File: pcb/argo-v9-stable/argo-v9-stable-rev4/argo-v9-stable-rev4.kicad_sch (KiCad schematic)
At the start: 131 parts, among them IC2 MP2672GD-0000, J1 Sparkfun_NEO-N9M-SMA, J2 USB4125-GF-A, J3 LED_power_button_RGB_LED, J4 Conn_I2C_Molex_705450003, J5 Conn_I2C_Molex_705450003, K1 PRL3-5V-DC-1A, Q1 BSD840N, Q2 BSD840N, SW1 ON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

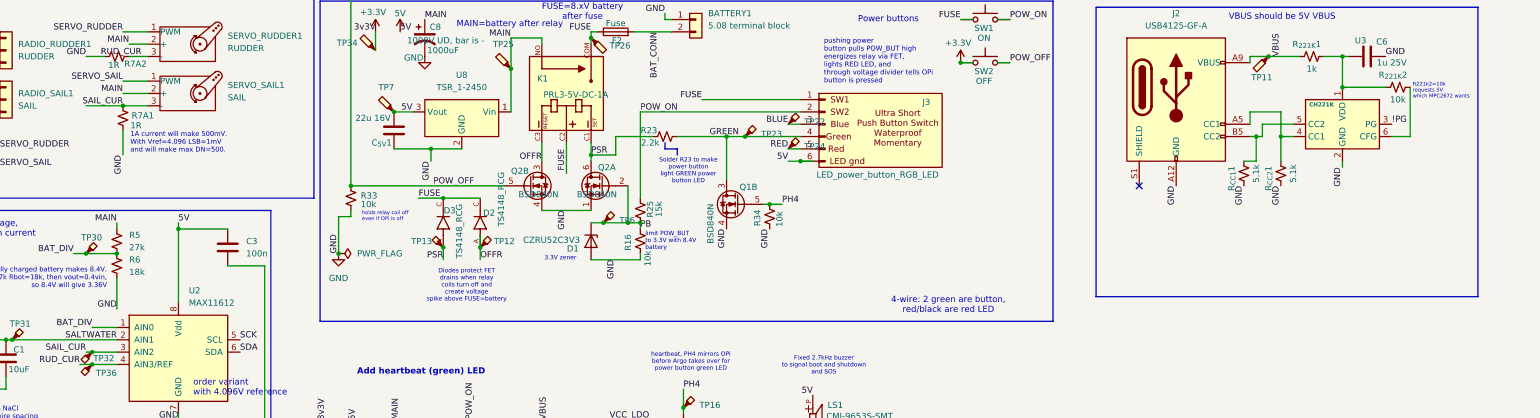
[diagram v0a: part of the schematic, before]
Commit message: add testpoints for CHG, CC1/2
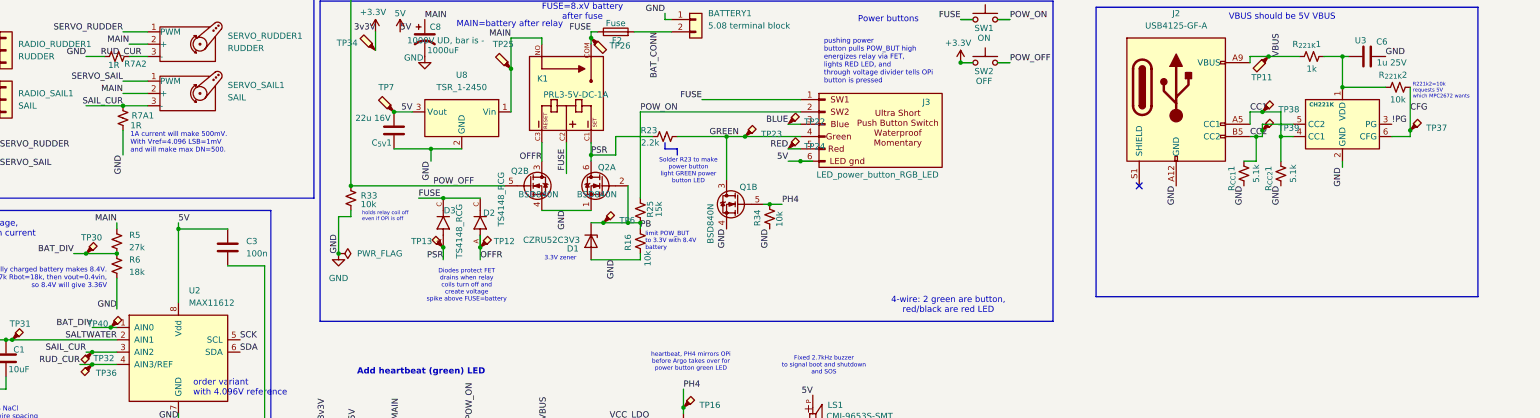
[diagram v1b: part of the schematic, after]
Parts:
- added TP37, TP38, TP39, TP40: TestPoint_Probe_autonamed, Argo footprint Library:TestPoint_scope_small_autonamed, symbol argo-v9:TestPoint_Probe_small_autonamed
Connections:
- net BAT_DIV: now also TP40.1
- net CC2: now reaches J2.B5 (CC2), R_{CC1}1.2, U3.5 (CC2)
- net CC2: now also TP39.1
- net CC1: now reaches J2.A5 (CC1), R_{CC2}1.2, U3.4 (CC1)
- net CC1: now also TP38.1
- net CFG: now reaches R_{221K}2.2, U3.6 (CFG)
- net CFG: now also TP37.1

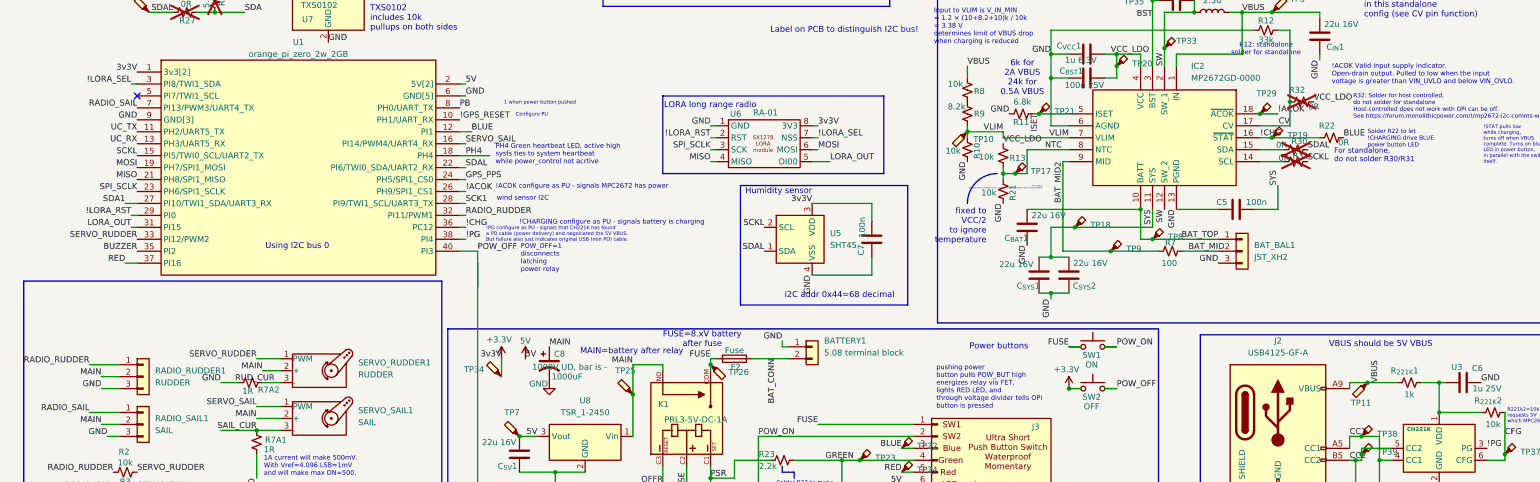
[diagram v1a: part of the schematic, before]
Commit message: more testpoints and cleanup text. Add libs
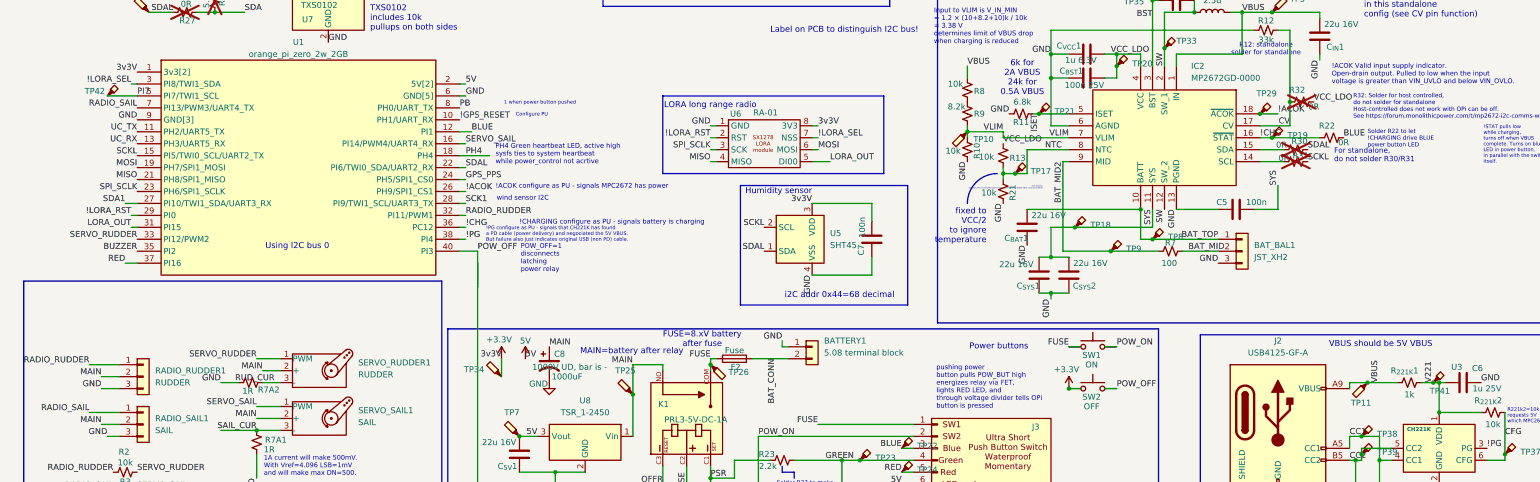
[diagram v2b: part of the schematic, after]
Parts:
- added TP41, TP42: TestPoint_Probe_autonamed, Argo footprint Library:TestPoint_scope_small_autonamed, symbol argo-v9:TestPoint_Probe_small_autonamed
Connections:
- net V221: now reaches C6.1, R_{221K}1.2, R_{221K}2.1, U3.1 (VDD)
- net V221: now also TP41.1
- net PI7: now reaches U1.5 (PI7/TWI1_SCL)
- net PI7: now also TP42.1
- no-connect marks 2 -> 1
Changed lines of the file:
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@@
 	)
 	(junction
+		(at 370.84 167.64)
+		(diameter 0)
+		(color 0 0 0 0)
+	)
+	(junction
 		(at 313.69 96.52)
 		(diameter 0)
@@
 	)
 	(no_connect
-		(at 95.25 106.68)
-	)
-	(no_connect
 		(at 330.2 194.31)
 	)
@@
 	(wire
 		(pts
+			(xy 370.84 167.64) (xy 372.11 167.64)
+		)
+		(stroke
+			(width 0)
+			(type default)
+		)
+	)
+	(wire
+		(pts
 			(xy 217.17 209.55) (xy 227.33 209.55)
 		)
@@
 	(wire
 		(pts
-			(xy 368.3 167.64) (xy 372.11 167.64)
+			(xy 368.3 167.64) (xy 370.84 167.64)
 		)
 		(stroke
@@
 	(wire
 		(pts
+			(xy 88.9 106.68) (xy 95.25 106.68)
+		)
+		(stroke
+			(width 0)
+			(type default)
+		)
+	)
+	(wire
+		(pts
 			(xy 209.55 77.47) (xy 204.47 77.47)
 		)
@@
 		)
 	)
+	(label "PI7"
+		(at 95.25 106.68 0)
+		(effects
+			(font
+				(size 1.27 1.27)
+			)
+			(justify left bottom)
+		)
+	)
 	(label "GND"
 		(at 232.41 158.75 180)
@@
 		)
 	)
+	(label "V221"
+		(at 370.84 167.64 90)
+		(effects
+			(font
+				(size 1.27 1.27)
+			)
+			(justify left bottom)
+		)
+	)
 	(label "5V"
 		(at 85.09 220.98 0)
@@
 	(symbol
 		(lib_id "argo-v9:TestPoint_Probe_small_autonamed")
+		(at 370.84 167.64 0)
+		(unit 1)
+		(exclude_from_sim no)
+		(in_bom no)
+		(on_board yes)
+		(dnp no)
+		(property "Reference" "TP41"
+			(at 370.078 169.418 0)
+			(effects
+				(font
+					(size 1.27 1.27)
+				)
+				(justify left)
+			)
+		)
+		(property "Value" "TestPoint_Probe_autonamed"
+			(at 372.491 163.576 0)
+			(effects
+				(font
+					(size 1.27 1.27)
+				)
+				(hide yes)
+			)
+		)
+		(property "Footprint" "Argo footprint Library:TestPoint_scope_small_autonamed"
+			(at 375.92 167.64 0)
+			(effects
+				(font
+					(size 1.27 1.27)
+				)
+				(hide yes)
+			)
+		)
+		(property "Datasheet" "~"
+			(at 375.92 167.64 0)
+			(effects
+				(font
+					(size 1.27 1.27)
+				)
+				(hide yes)
+			)
+		)
+		(property "Description" "test point (alternative probe-style design)"
+			(at 370.84 167.64 0)
+			(effects
+				(font
+					(size 1.27 1.27)
+				)
+				(hide yes)
+			)
+		)
+		(pin "1"
+		)
+		(instances
+			(project "argo-v9-stable-rev4"
+				(path "/94ef8c18-8f4d-4fb8-af3c-a2b214cf3496"
+					(reference "TP41")
+					(unit 1)
+				)
+			)
+		)
+	)
+	(symbol
+		(lib_id "argo-v9:TestPoint_Probe_small_autonamed")
 		(at 313.69 96.52 0)
 		(unit 1)
@@
 					(unit 1)
 				)
+			)
+		)
+	)
+	(symbol
+		(lib_id "argo-v9:TestPoint_Probe_small_autonamed")
+		(at 88.9 106.68 0)
+		(unit 1)
+		(exclude_from_sim no)
+		(in_bom no)
+		(on_board yes)
+		(dnp no)
+		(property "Reference" "TP42"
+			(at 84.074 105.664 0)
+			(effects
+				(font
+					(size 1.27 1.27)
+				)
+				(justify left)
+			)
+		)
+		(property "Value" "TestPoint_Probe_autonamed"
+			(at 90.551 102.616 0)
+			(effects
+				(font
+					(size 1.27 1.27)
+				)
+				(hide yes)
+			)
+		)
+		(property "Footprint" "Argo footprint Library:TestPoint_scope_small_autonamed"
+			(at 93.98 106.68 0)
+			(effects
+				(font
+					(size 1.27 1.27)
+				)
+				(hide yes)
+			)
+		)
+		(property "Datasheet" "~"
+			(at 93.98 106.68 0)
+			(effects
+				(font
+					(size 1.27 1.27)
+				)
+				(hide yes)
+			)
+		)
+		(property "Description" "test point (alternative probe-style design)"
+			(at 88.9 106.68 0)
+			(effects
+				(font
+					(size 1.27 1.27)
+				)
+				(hide yes)
+			)
+		)
+		(pin "1"
+		)
+		(instances
+			(project "argo-v9-stable-rev4"
+				(path "/94ef8c18-8f4d-4fb8-af3c-a2b214cf3496"
+					(reference "TP42")
+					(unit 1)
+				)

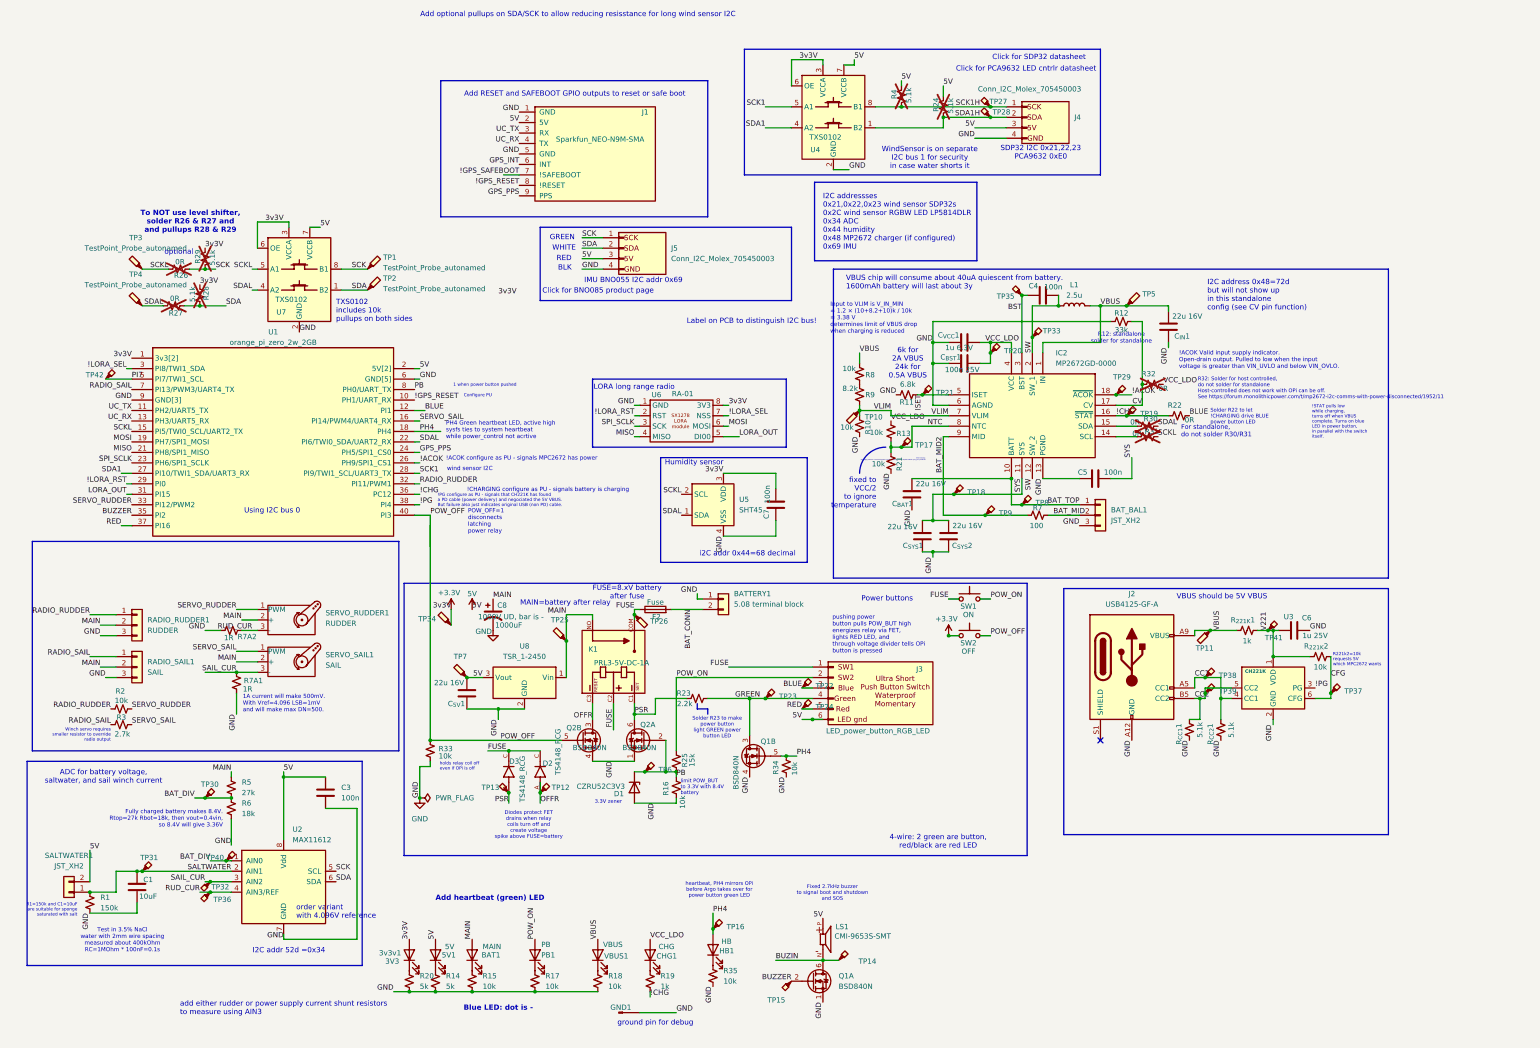
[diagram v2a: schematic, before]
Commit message: jlcpcb fabricated versions of latest PCBs (rev4 argo and rev1c windsensor). For assembly on return to Zurich
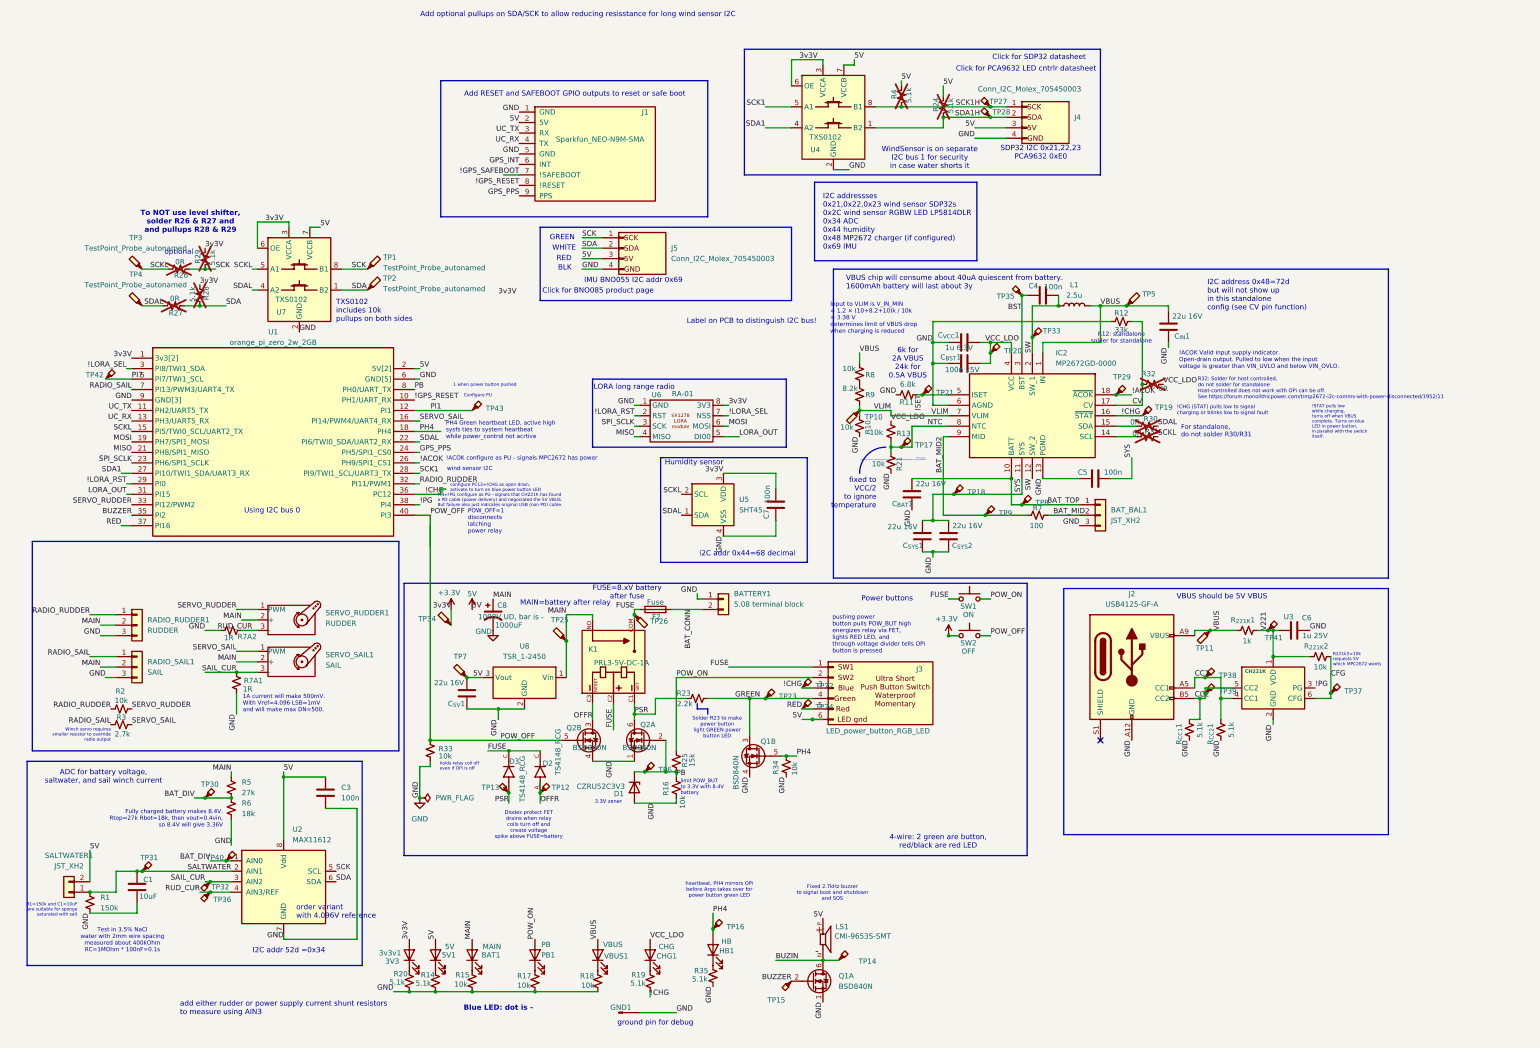
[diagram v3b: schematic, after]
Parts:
- removed R22: 0R, Resistor_SMD:R_0603_1608Metric_Pad0.98x0.95mm_HandSolder, symbol Device:R_Small_US
- added TP43: TestPoint_Probe_autonamed, Argo footprint Library:TestPoint_scope_small_autonamed, symbol argo-v9:TestPoint_Probe_small_autonamed
- R14, R20: value 5k -> 5.1k
- R19: value 1k -> 5.1k
- R35: value 10k -> 5.1k
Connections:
- net !CHG: now also J3.3 (Pin_3), TP22.1
- removed net BLUE: J3.3 (Pin_3), TP22.1, U1.12 (PI1)
- new net PI1: TP43.1, U1.12 (PI1)
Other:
- note added: "!CHG (STAT) pulls low to signal charging or blinks low to signal fault"
- note added: "PI4=!PG configure as PU - signals that CH221K has found a PD cable (power delivery) and negociated the 5V VBUS. But failure also just indicates original USB (non PD) cable."
- note added: "configure PC12=!CHG as open drain, activate to turn on blue power button LED"
- note removed: "!CHARGING configure as PU - signals battery is charging"
- note removed: "!PG configure as PU - signals that CH221K has found a PD cable (power delivery) and negociated the 5V VBUS. But failure also just indicates original USB (non PD) cable."
- note removed: "Add heartbeat (green) LED"
- note removed: "Solder R22 to let !CHARGING drive BLUE power button LED"
- moved on the sheet: TP19
